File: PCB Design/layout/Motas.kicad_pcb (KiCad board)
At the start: 2 copper layers, 63.2 x 37.8 mm, 27 parts

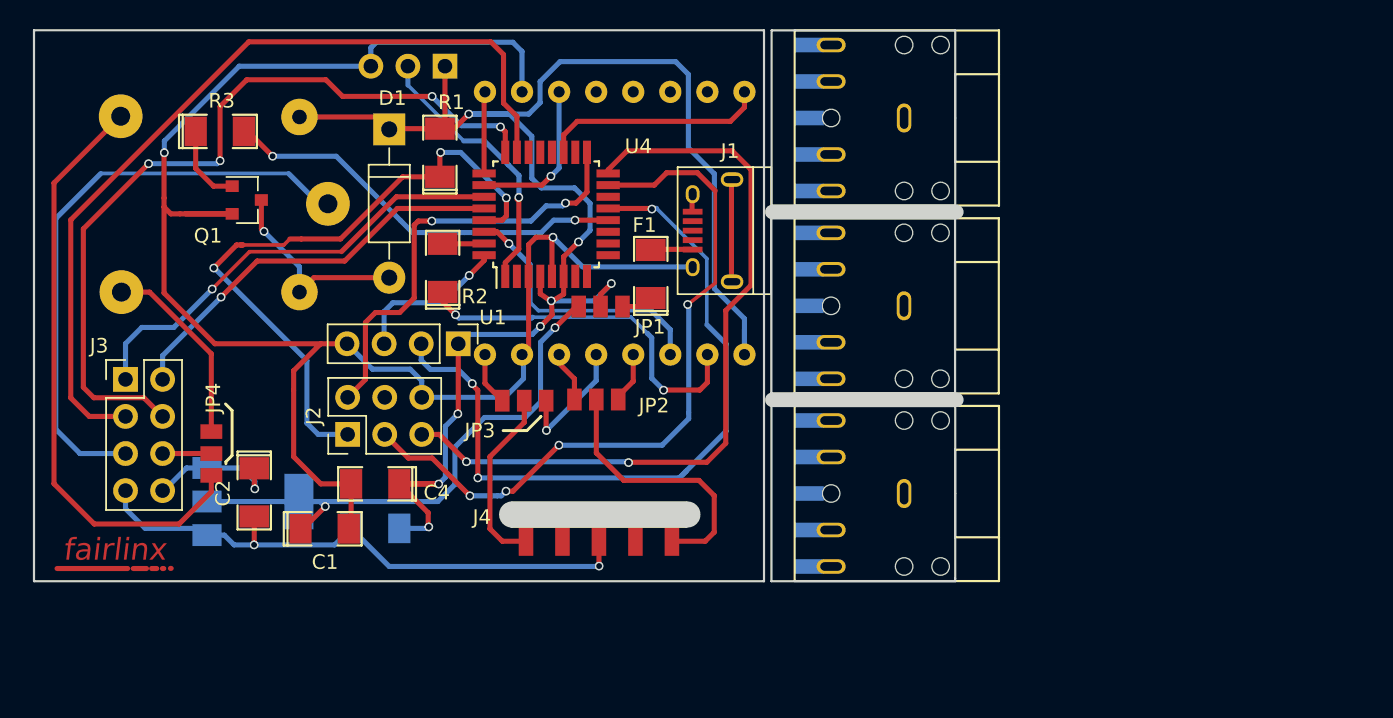
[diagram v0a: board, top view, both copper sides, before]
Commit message: added software uart
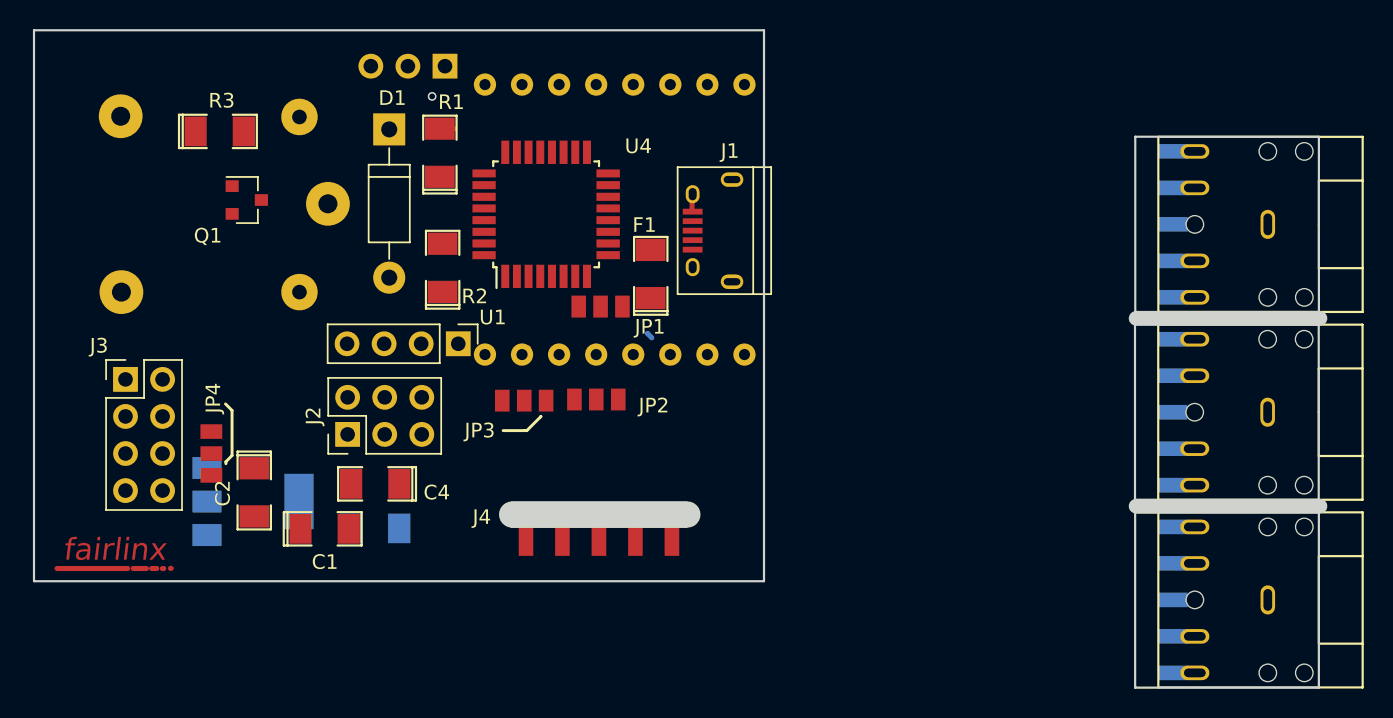
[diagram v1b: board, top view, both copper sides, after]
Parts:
- moved ? 26.0 mm to (208.3, 130.0)
- moved ? 26.0 mm to (208.3, 142.9)
- moved ? 26.0 mm to (208.3, 117.2)
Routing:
- net GND: track 167.1 -> 1.44 mm, vias 4 -> 0
- net +5V: track 115.8 -> 3.74 mm, vias 8 -> 0
- net GPIO1: track 58.6 -> 0.00 mm
- net GPIO2: track 55.3 -> 0.00 mm, vias 4 -> 0
- net MISO: track 52.8 -> 0.00 mm, vias 2 -> 0
- net TRIG_CONTRL: track 51.5 -> 0.00 mm, vias 3 -> 0
- net MOSI: track 49.5 -> 0.00 mm, vias 4 -> 0
- net RST: track 45.0 -> 0.00 mm, vias 3 -> 0
- net Net-(JP4-Pad1): track 41.0 -> 0.00 mm
- net RL_OUT_1: track 40.7 -> 0.62 mm
- net Net-(C1-Pad1): track 39.7 -> 0.34 mm, vias 2 -> 0
- net GPIO3/DBG_TX: track 31.2 -> 0.00 mm, vias 1 -> 0
- net SCK: track 30.2 -> 0.00 mm, vias 2 -> 0
- net RL_CONTRL: track 28.2 -> 0.27 mm, vias 2 -> 0
- net GPIO4/DBG_RX: track 27.8 -> 0.00 mm, vias 1 -> 0
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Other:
- board size 63.2 x 37.8 mm -> 88.1 x 45 mm
